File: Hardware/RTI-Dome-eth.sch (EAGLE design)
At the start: 78 parts, among them IC1 24AA128ST, IC3 FT232RL, IC5 74LVC245, IC6 74ABT245, J1 POWERPOLE_POWER45A, U1 W5500, X13 PN61729-S, X9 J1011F21PNL

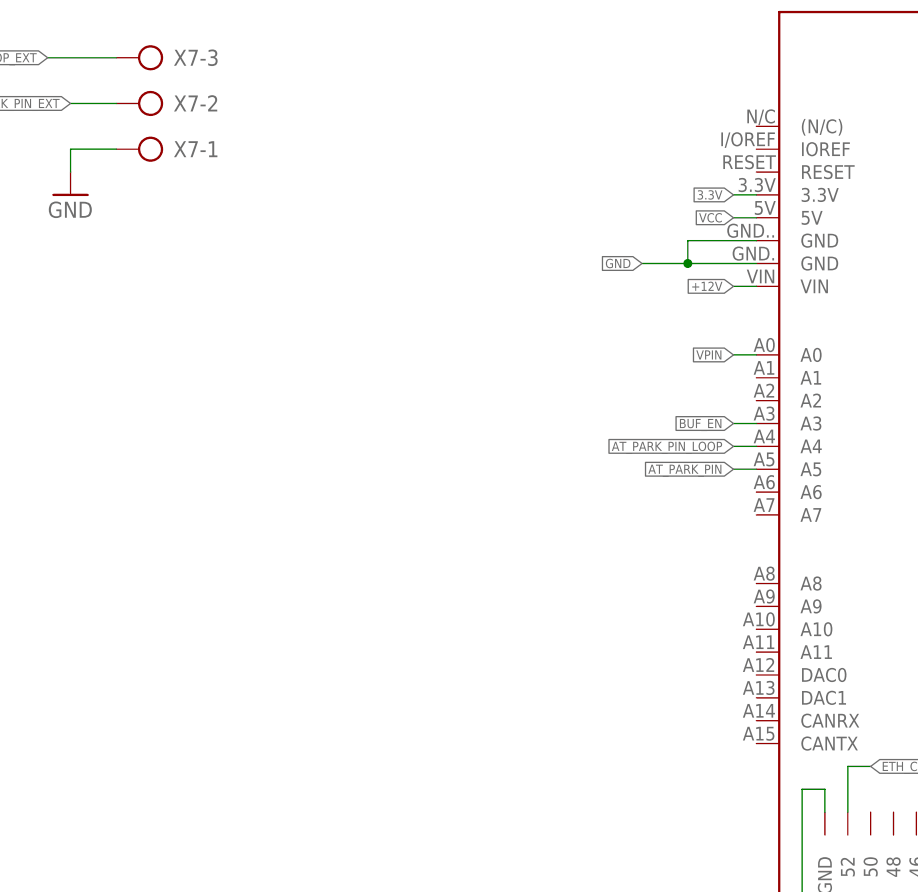
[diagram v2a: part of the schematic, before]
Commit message: Adding MCP120 for power on reset.
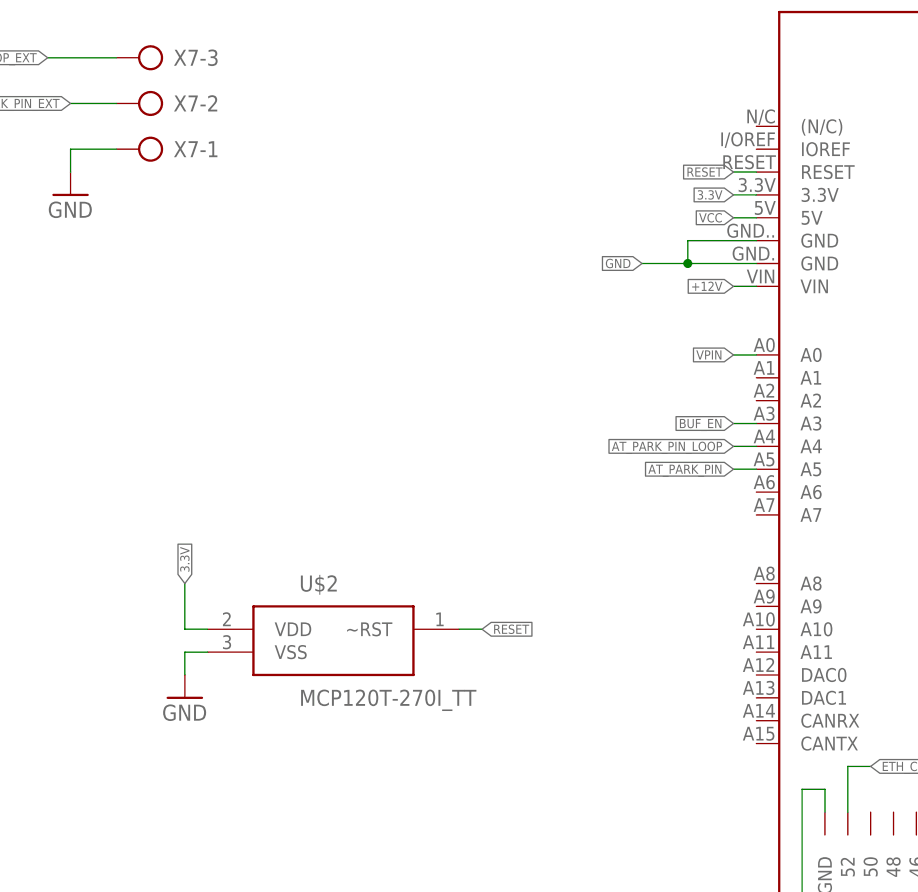
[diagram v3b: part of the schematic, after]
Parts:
- added U$2: MCP120T-270I_TT, MCP120T-270I_TT:MCP120T-270I_TT
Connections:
- new net RESET: U$1.RESET, U$2.~RST
- net 3.3V: now also U$2.VDD
- net GND: now also U$2.VSS
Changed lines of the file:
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@@
 <part name="GND17" library="supply1" deviceset="GND" device=""/>
 <part name="R30" library="rti" deviceset="R-EU" device="'0805'" value="4.7K"/>
+<part name="U$2" library="MCP120T-270I_TT" deviceset="MCP120T-270I_TT" device=""/>
+<part name="GND18" library="supply1" deviceset="GND" device=""/>
 </parts>
 <sheets>
@@
 <instance part="GND17" gate="1" x="596.9" y="104.14"/>
 <instance part="R30" gate="G$1" x="469.9" y="129.54" rot="R270"/>
+<instance part="U$2" gate="G$1" x="53.34" y="63.5"/>
+<instance part="GND18" gate="1" x="38.1" y="55.88"/>
 </instances>
 <busses>
@@
 <pinref part="GND17" gate="1" pin="GND"/>
 </segment>
+<segment>
+<pinref part="U$2" gate="G$1" pin="VSS"/>
+<wire x1="40.64" y1="60.96" x2="38.1" y2="60.96" width="0.1524" layer="91"/>
+<wire x1="38.1" y1="60.96" x2="38.1" y2="58.42" width="0.1524" layer="91"/>
+<pinref part="GND18" gate="1" pin="GND"/>
+</segment>
 </net>
 <net name="+12V" class="1">
@@
 <junction x="596.9" y="127"/>
 <label x="599.44" y="127" size="1.016" layer="95" xref="yes"/>
+</segment>
+<segment>
+<pinref part="U$2" gate="G$1" pin="VDD"/>
+<wire x1="40.64" y1="63.5" x2="38.1" y2="63.5" width="0.1524" layer="91"/>
+<wire x1="38.1" y1="63.5" x2="38.1" y2="68.58" width="0.1524" layer="91"/>
+<label x="38.1" y="68.58" size="1.016" layer="95" rot="R90" xref="yes"/>
 </segment>
 </net>
@@
 </segment>
 </net>
+<net name="RESET" class="0">
+<segment>
+<pinref part="U$2" gate="G$1" pin="~RST"/>
+<wire x1="71.12" y1="63.5" x2="68.58" y2="63.5" width="0.1524" layer="91"/>
+<label x="71.12" y="63.5" size="1.016" layer="95" xref="yes"/>
+</segment>
+<segment>
+<pinref part="U$1" gate="G$1" pin="RESET"/>
+<wire x1="99.06" y1="114.3" x2="101.6" y2="114.3" width="0.1524" layer="91"/>
+<label x="99.06" y="114.3" size="1.016" layer="95" rot="R180" xref="yes"/>
+</segment>
+</net>

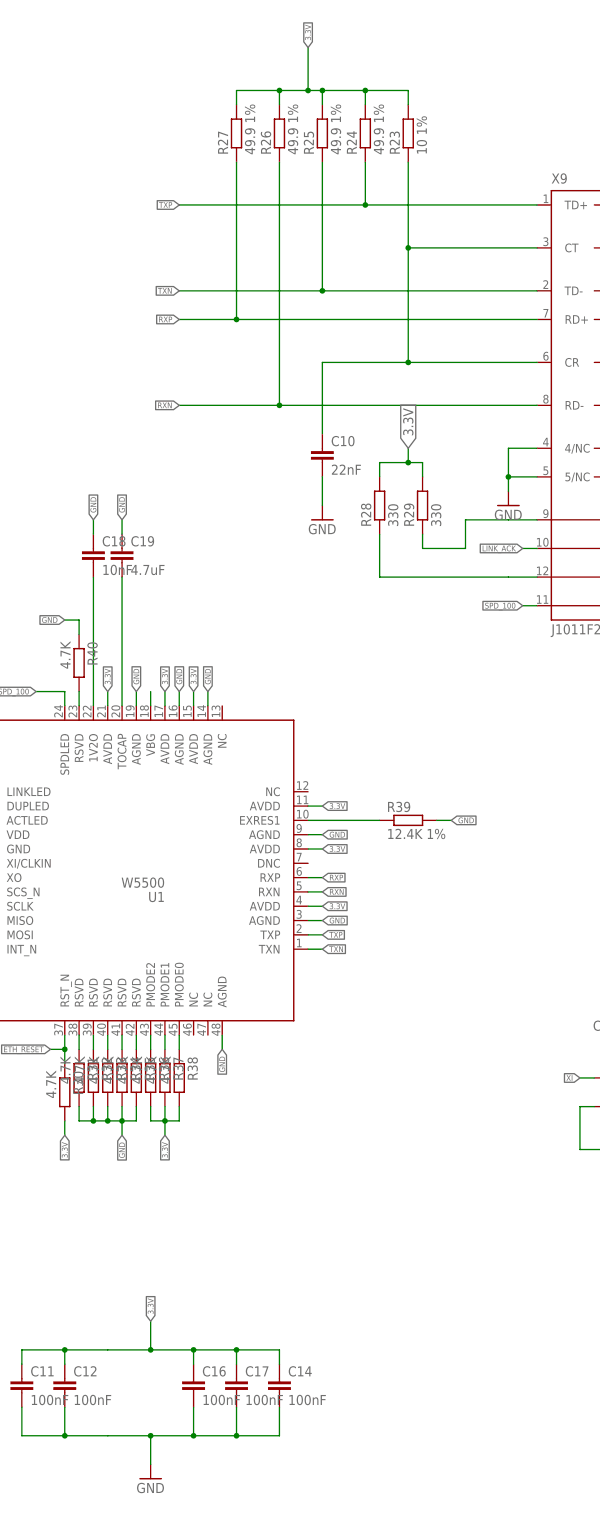
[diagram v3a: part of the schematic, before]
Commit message: Redid the analog 3.3V on the ethernet shield
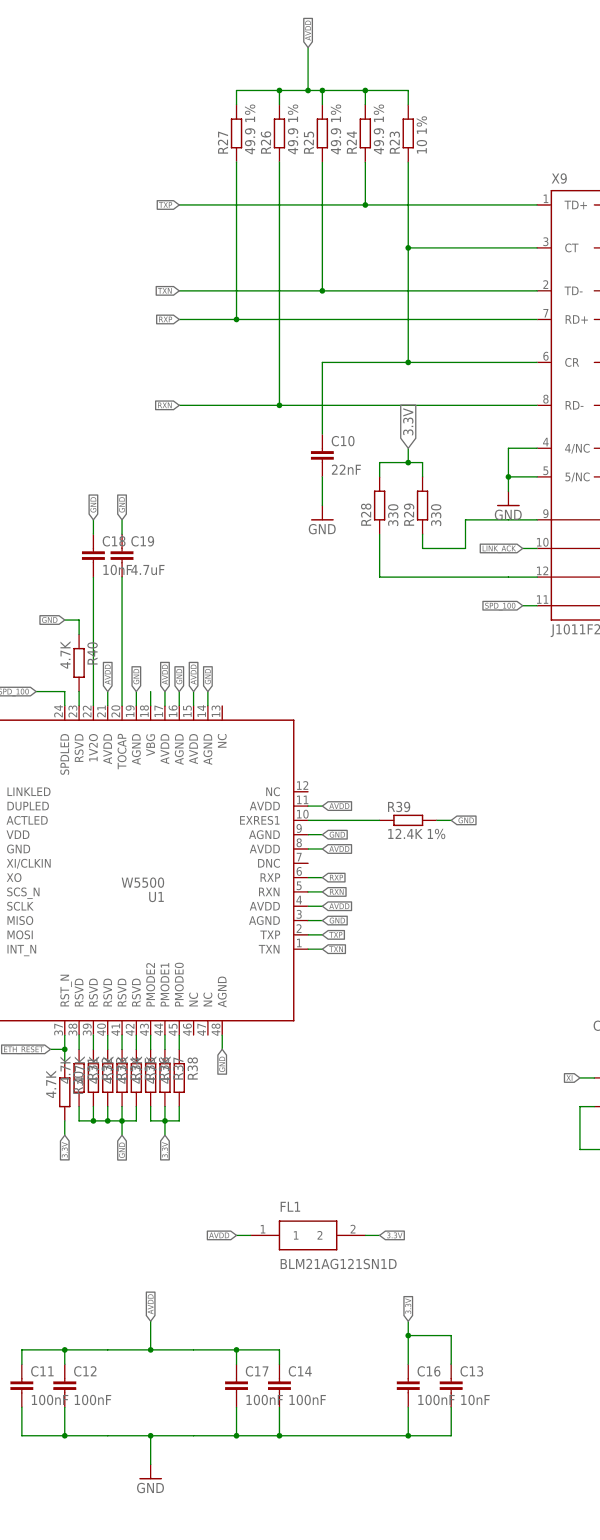
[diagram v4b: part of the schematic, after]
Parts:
- added C13: 10nF, rti:C-EU'0805'
- added FL1: BLM21AG121SN1D, BLM21AG121SN1D:BLM21AG121SN1D
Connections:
- new net AVDD: C11.1, C12.1, C14.1, C17.1, FL1.1, R23.2, R24.2, R25.2, R26.2, R27.2, U1.AVDD@1, U1.AVDD@2, U1.AVDD@3, U1.AVDD@4, U1.AVDD@5, U1.AVDD@6
- net 3.3V: now also C13.1, FL1.2; no longer C11.1, C12.1, C14.1, C17.1, R23.2, R24.2, R25.2, R26.2, R27.2, U1.AVDD@1, U1.AVDD@2, U1.AVDD@3, U1.AVDD@4, U1.AVDD@5, U1.AVDD@6
- net GND: now also C13.2
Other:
- moved on the sheet: C16

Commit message: Fix some routing
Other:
- moved on the sheet: C18
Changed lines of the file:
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@@
 <instance part="C17" gate="G$1" x="500.38" y="78.74"/>
 <instance part="GND14" gate="1" x="485.14" y="60.96"/>
-<instance part="C18" gate="G$1" x="474.98" y="226.06"/>
+<instance part="C18" gate="G$1" x="474.98" y="218.44"/>
 <instance part="R28" gate="G$1" x="525.78" y="233.68" rot="R90"/>
 <instance part="R29" gate="G$1" x="533.4" y="233.68" rot="R90"/>
@@
 <segment>
 <pinref part="C18" gate="G$1" pin="1"/>
-<wire x1="474.98" y1="231.14" x2="474.98" y2="228.6" width="0.1524" layer="91"/>
+<wire x1="474.98" y1="231.14" x2="474.98" y2="220.98" width="0.1524" layer="91"/>
 <label x="474.98" y="231.14" size="1.016" layer="95" rot="R90" xref="yes"/>
 </segment>
@@
 <segment>
 <pinref part="U1" gate="G$1" pin="1V2O"/>
-<wire x1="474.98" y1="220.98" x2="474.98" y2="198.12" width="0.1524" layer="91"/>
+<wire x1="474.98" y1="213.36" x2="474.98" y2="198.12" width="0.1524" layer="91"/>
 <pinref part="C18" gate="G$1" pin="2"/>
 </segment>

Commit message: Better homing code. Does necessarily stop at home bug sinf home via an interrupt. I'll add more got to go back home after passing it. It does however return the proper position after homing. Added more board for ENC424J600 ethernet chip. Fix position of the headers.
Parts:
- added C15, C21: 6.8nF, rti:C-EU'0805'
- added C22: 10nF, rti:C-EU'0805'
- added C25, C26: 10uF, rti:C-EU'1206'
- added IC4: REG1117, burr-brown:REG1117
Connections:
- new net +3V3: 25MHZ.OE, 25MHZ.VDD, C13.1, C16.1, C20.1, C26.1, C9.1, FL1.2, IC3.VCCIO, IC4.VOUT, R28.2, R29.2, R30.2, R36.2, R37.2, R38.2, U1.VDD
- new net N$11: C15.2, X9.RD+
- new net N$12: C21.2, X9.RD-
- new net N$13: C10.1, R23.1, X9.CT
- net 3.3V: no longer 25MHZ.OE, 25MHZ.VDD, C13.1, C16.1, C20.1, C9.1, FL1.2, IC3.VCCIO, R28.2, R29.2, R30.2, R36.2, R37.2, R38.2, U1.VDD
- net AVDD: no longer R26.2, R27.2
- net GND: now also C22.2, C25.2, C26.2, IC4.GND, X9.CGND, X9.CGND2
- net N$7: now also C22.1, R26.2, R27.2; no longer C10.1, R23.1, X9.CT
- net RXN: now also C21.1; no longer X9.RD-
- net RXP: now also C15.1; no longer X9.RD+
- net VCC: now also C25.1, IC4.VIN
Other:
- moved on the sheet: C10, C9, R26, R27
